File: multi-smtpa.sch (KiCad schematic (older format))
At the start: 72 parts, among them J1 Screw_Terminal_01x02, J10 J SMTPA, J11 Screw_Terminal_01x02, J2 J SMTPA, J3 J SMTPA, J4 J SMTPA, J5 J SMTPA, J6 J SMTPA, J7 J SMTPA, J8 J SMTPA, J9 J SMTPA, U1 LM317L_SO8, U2 LM317L_SO8, U3 LM317L_SO8, U4 LM317L_SO8, U5 LM317L_SO8, U6 LM317L_SO8, U7 LM317L_SO8, U8 LM317L_SO8, U9 LM317L_SO8

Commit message: eval board done
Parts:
- removed F?: Fuse_Small 5A, symbol Device:Fuse_Small
- removed J10, J5, J8, J9: J SMTPA, footprints:SMTPA J30035, symbol Connector_Generic:Conn_01x05
- removed J11, J? (x4): Screw_Terminal_01x02, symbol Connector:Screw_Terminal_01x02
- removed R17, R18: 240R, symbol Device:R
- removed RV8, RV9: R_POT_TRIM, symbol Device:R_POT_TRIM
- removed U5, U9: LM317L_SO8, Package_SO:SOIC-8_3.9x4.9mm_P1.27mm, symbol Regulator_Linear:LM317L_SO8
- added C21, C27, C28, C36, C39, C45, C48, C53, C54: 1n, Capacitor_SMD:C_0603_1608Metric_Pad1.05x0.95mm_HandSolder, symbol Device:C
- added C22: 68p, Capacitor_SMD:C_0603_1608Metric_Pad1.05x0.95mm_HandSolder, symbol Device:C
- added C23, C24, C34, C37, C4, C43, C46, C49, C50, C8: 100n, Capacitor_SMD:C_0603_1608Metric_Pad1.05x0.95mm_HandSolder, symbol Device:C
- added C25, C26, C35, C38, C44, C47, C51, C52: 10n, Capacitor_SMD:C_0603_1608Metric_Pad1.05x0.95mm_HandSolder, symbol Device:C
- added C29, C33, C42: 1u, Capacitor_SMD:C_0805_2012Metric_Pad1.15x1.40mm_HandSolder, symbol Device:C
- added C30, C32, C41: 0.1u, Capacitor_SMD:C_0805_2012Metric_Pad1.15x1.40mm_HandSolder, symbol Device:C
- added C31, C40: 10n, Capacitor_SMD:C_0603_1608Metric_Pad1.05x0.95mm_HandSolder, symbol Device:C_Small
- added C55, C57: 100p, Capacitor_SMD:C_0402_1005Metric, symbol Device:C
- added C56, C58: 10p, Capacitor_SMD:C_0402_1005Metric, symbol Device:C
- added D2, D3, D4, D5, D6, D7: D_Schottky_x2_Serial_AKC, Package_TO_SOT_SMD:SOT-23, symbol Device:D_Schottky_x2_Serial_AKC
- added H1, H2, H3, H4: MountingHole, MountingHole:MountingHole_4.3mm_M4_DIN965_Pad, symbol Mechanical:MountingHole
- added J10, J13, J15, J18, J19, J21, J5, J8, J9: Conn_Coaxial, Connector_Coaxial:SMA_Amphenol_132289_EdgeMount, symbol Connector:Conn_Coaxial
- added J11, J12, J14, J16, J17, J20: J SMTPA, footprints:SMTPA J30035, symbol Connector_Generic:Conn_01x05
- added L1: 43n, Inductor_SMD:L_0402_1005Metric, symbol Device:L
- added U5: ADL5610, Package_TO_SOT_SMD:SOT-89-3, symbol RF_Amplifier:ADL5610
- C1, C12, C2, C3, C5, C6, C7, C9: footprint (none) -> Capacitor_SMD:C_0805_2012Metric_Pad1.15x1.40mm_HandSolder
- C10: value 0.1u -> 100n; footprint (none) -> Capacitor_SMD:C_0603_1608Metric_Pad1.05x0.95mm_HandSolder
- C11: value 0.1u -> 2u2T; footprint (none) -> Capacitor_SMD:C_0805_2012Metric_Pad1.15x1.40mm_HandSolder
- C13, C14: value 1u -> 10n; footprint (none) -> Capacitor_SMD:C_0603_1608Metric_Pad1.05x0.95mm_HandSolder
- C15: value 0.1u -> 10n; footprint (none) -> Capacitor_SMD:C_0603_1608Metric_Pad1.05x0.95mm_HandSolder
- C16: value 0.1u -> 1.2n; footprint (none) -> Capacitor_SMD:C_0603_1608Metric_Pad1.05x0.95mm_HandSolder
- C17: value 0.1u -> 100p; footprint (none) -> Capacitor_SMD:C_0603_1608Metric_Pad1.05x0.95mm_HandSolder
- C18: value 1u -> 100p; footprint (none) -> Capacitor_SMD:C_0603_1608Metric_Pad1.05x0.95mm_HandSolder
- C19, C20: value 1u -> 1n; footprint (none) -> Capacitor_SMD:C_0603_1608Metric_Pad1.05x0.95mm_HandSolder
- D1: footprint (none) -> Diode_THT:D_A-405_P10.16mm_Horizontal
- F1: renamed from F?; value Fuse_Small -> Fuse 1A fast; footprint (none) -> Resistor_THT:R_Axial_DIN0207_L6.3mm_D2.5mm_P10.16mm_Horizontal
- J1: footprint (none) -> TerminalBlock_TE-Connectivity:TerminalBlock_TE_282834-2_1x02_P2.54mm_Horizontal
- R1, R10, R15, R16, R2, R3, R4, R5, R6, R7: footprint (none) -> Resistor_SMD:R_0805_2012Metric_Pad1.15x1.40mm_HandSolder
- R11: value 240R -> 1K0; footprint (none) -> Resistor_SMD:R_0603_1608Metric_Pad1.05x0.95mm_HandSolder
- R12: value 240R -> 1K0; footprint (none) -> Resistor_SMD:R_0805_2012Metric_Pad1.15x1.40mm_HandSolder
- R13, R9: value 1K0 -> 240R; footprint (none) -> Resistor_SMD:R_0805_2012Metric_Pad1.15x1.40mm_HandSolder
- R14: footprint (none) -> Resistor_SMD:R_0603_1608Metric_Pad1.05x0.95mm_HandSolder
- R8: value 1K0 -> 22R; footprint (none) -> Resistor_SMD:R_0603_1608Metric_Pad1.05x0.95mm_HandSolder
- RV1, RV2, RV3, RV4, RV5, RV6, RV7: footprint (none) -> Potentiometer_THT:Potentiometer_Bourns_3006Y_Horizontal
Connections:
- net VDC_22 is gone; now on net VDC_10: C20.1
- net +48V: now also D1.2 (A), C30.1, C32.1, C41.1; no longer C10.1, C11.1, C15.1, C16.1, C17.1, D1.1 (K)
- net Fast_00: now also J5.1 (In)
- net Fast_01: now also J10.1 (In)
- net Fast_10: now also D3.3 (common)
- net Fast_11: now also D2.3 (common)
- net Fast_20: now also C17.2
- net Fast_21: now also J17.2 (Pin_2), J18.1 (In)
- net Fast_22: now also J19.1 (In), J20.2 (Pin_2)
- net GND: now also C11.1, C14.2, C15.2, C16.1, C19.2, C20.2, C3.2, C7.2, R12.2, R15.2, R3.2, RV5.3, C21.2, C22.1, C23.2, C24.2, C25.2, C26.2, C27.2, C28.2, C29.2, C30.2, C32.2, C33.2, C34.2, C35.2, C36.2, C37.2, C38.2, C39.2, C4.2, C41.2, C42.2, C43.2, C44.2, C45.2, C46.2, C47.2, C48.2, C49.2, C50.2, C51.2, C52.2, C53.2, C54.2, C55.2, C56.2, C57.2, C58.2, C8.2, D2.1 (A), D3.1 (A), D4.1 (A), D5.1 (A), D6.1 (A), D7.1 (A), J10.2 (Ext), J11.1 (Pin_1), J11.4 (Pin_4), J11.5 (Pin_5), J12.1 (Pin_1), J12.4 (Pin_4), J12.5 (Pin_5), J13.2 (Ext), J14.1 (Pin_1), J14.4 (Pin_4), J14.5 (Pin_5), J15.2 (Ext), J16.1 (Pin_1), J16.4 (Pin_4), J16.5 (Pin_5), J17.1 (Pin_1), J17.4 (Pin_4), J17.5 (Pin_5), J18.2 (Ext), J19.2 (Ext), J20.1 (Pin_1), J20.4 (Pin_4), J20.5 (Pin_5), J21.2 (Ext), J5.2 (Ext), J8.2 (Ext), J9.2 (Ext), U5.2 (GND); no longer R8.2
- net VDC_00: now also C13.1, C19.1, C4.1, C55.1, C56.1
- net VDC_01: now also C23.1, C25.1, C27.1
- net VDC_10: now also C14.1, J7.3 (Pin_3), C24.1, C26.1, C28.1, C8.1
- net VDC_20: now also C10.1, C15.1, C21.1
- net VDC_21: now also R13.2, U7.2 (VO), U7.3 (VO), U7.6 (VO), U7.7 (VO), C33.1, C34.1, C35.1, C36.1, C37.1, C38.1, C39.1, C57.1, C58.1, J17.3 (Pin_3), J20.3 (Pin_3); no longer C14.1, R12.2, U6.2 (VO), U6.3 (VO), U6.6 (VO), U6.7 (VO)
- net at RV5.2: now also R9.1, U6.4 (ADJ); no longer R11.1
- net TEEBFast_20: now reaches R8.1
- net TEEBFast_20: now also R9.2, U6.2 (VO), U6.3 (VO), U6.6 (VO), U6.7 (VO), C29.1; no longer RV5.3
- net at RV6.3: now also R12.1; no longer R9.1
- net at R16.1, RV7.2: now also U8.4 (ADJ); no longer U7.4 (ADJ)
- net at R13.1: now also RV6.2, U7.4 (ADJ); no longer RV7.3
- net VssFast_lin: now reaches R14.1
- net VssFast_lin: now also J21.1 (In)
- net at R15.1: now also RV7.3
- net at F1.1: now also D1.1 (K); no longer D1.2 (A)
- removed net VDC_02: C18.1, R16.2, U7.2 (VO), U7.3 (VO), U7.6 (VO), U7.7 (VO)
- removed net VDC_11: C13.1, J7.3 (Pin_3), R11.2
- net VDC_12 renamed VDC_lin
- net VDC_lin: now also R16.2, C42.1, C43.1, C44.1, C45.1, C46.1, C47.1, C48.1, C49.1, C50.1, C51.1, C52.1, C53.1, C54.1, J11.3 (Pin_3), J12.3 (Pin_3), J14.3 (Pin_3), J16.3 (Pin_3); no longer C19.1
- new net AFast_20: C18.2, J8.1 (In)
- new net ATEEFast_20: C18.1, L1.2, U5.3
- new net CFast_1X: C31.1, J9.1 (In)
- new net CFast_lin: C40.1, J13.1 (In)
- new net Fast_1X: C31.2, D2.2 (K), D3.2 (K), R11.2
- new net Fast_lin: C40.2, D4.2 (K), D5.2 (K), D6.2 (K), D7.2 (K), R14.2
- new net Fast_lin0: D4.3 (common), J11.2 (Pin_2)
- new net Fast_lin1: D5.3 (common), J14.2 (Pin_2)
- new net Fast_lin2: D6.3 (common), J12.2 (Pin_2)
- new net Fast_lin3: D7.3 (common), J16.2 (Pin_2)
- new net PAFast_20: C17.1, U5.1
- new net TEEAFast_20: C11.2, C16.2, C22.2, L1.1, R8.2
- new net VssFast_1X: J15.1 (In), R11.1
- no-connect marks 9 -> 7
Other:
- note added: "Amplified Output"
- note added: "Linear Array of Four SiPMs, Signal Mux'd with Diodes, Tight Pack"
- note added: "Power"
- note added: "Sbias voltage and this applies a forward bias across the Schottky diodes.\n A 1kOhm resistor, Rs, is placed in series with Sbias at the Common Readout node.\nThe bias voltage is adjusted such that an optimal standing current of <1mA per Shottky diode is set up."
- note added: "Single SiPM, Amplified Output Experiment"
- note added: "Two SiPMs Mux'd with Diodes Experiment, Diode Under SiPM"
- note added: "Two SiPMs, One Power Source Experiment"
- note added: "Two SiPMs, individual Power Source, Differing Caps & Layout Experiment"
- note added: "approx 50 mA max @ 28V PER SiPM\napprox 14 Watts @ 0.5A total"
- note removed: "apply variable voltage 5-12.6V \nfan 603-1025-ND\n500mA"
- note removed: "approx 50 mA max @ 28V\napprox 14 Watts @ 0.5A total"
- moved on the sheet: C1, C12, C2, C3, C5, C6, C7, C9, D1, F1, J1, J2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

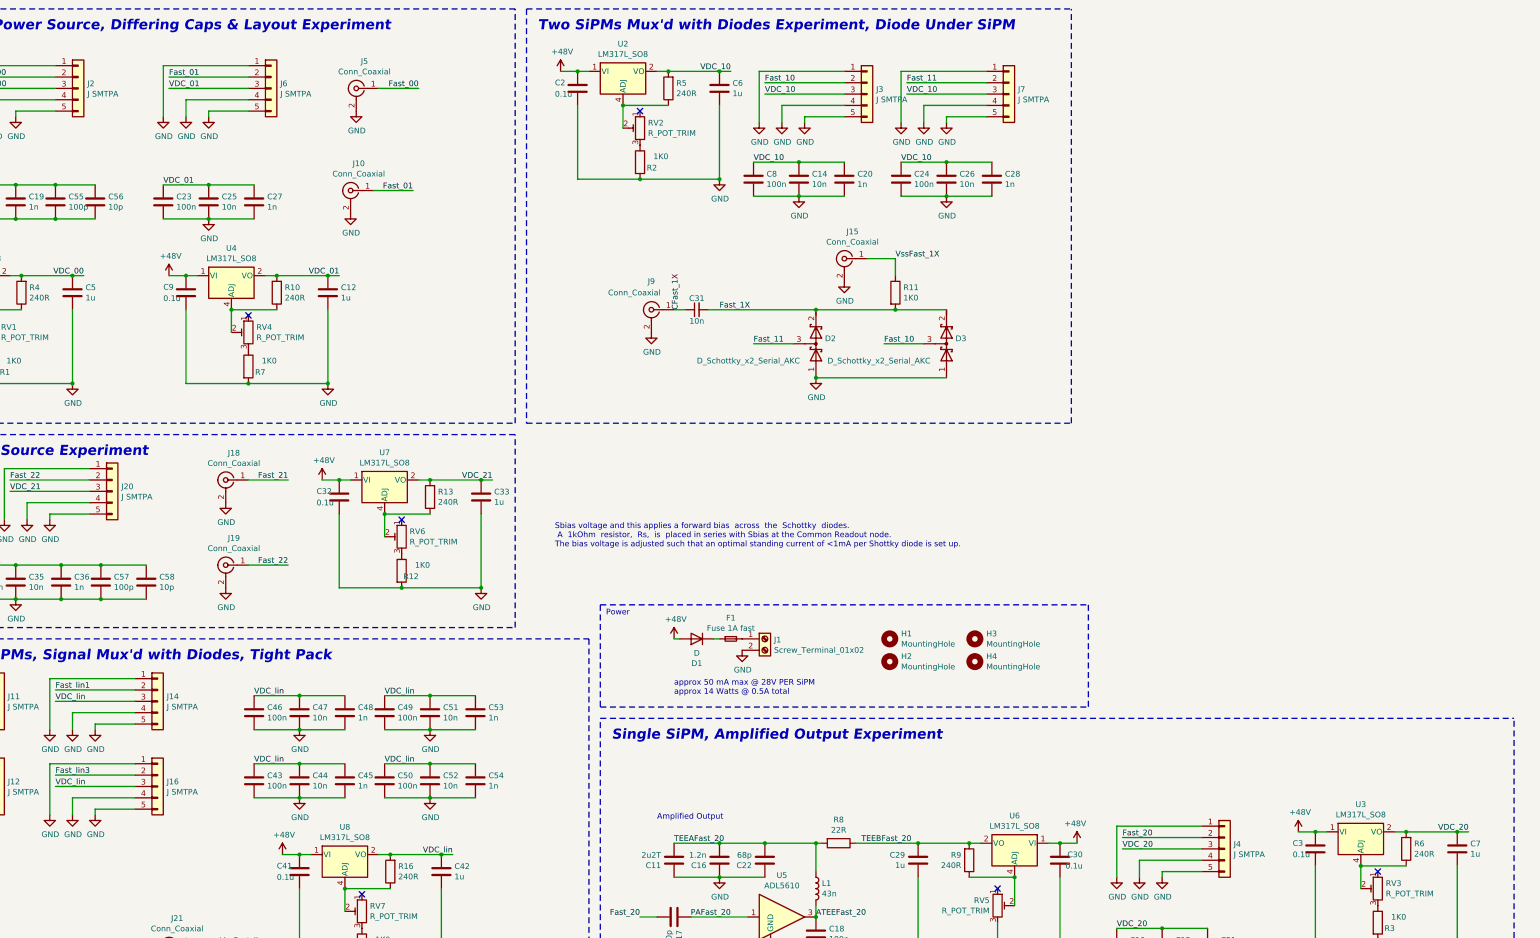
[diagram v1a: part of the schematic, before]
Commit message: added another experiment, testpoints, fiducials
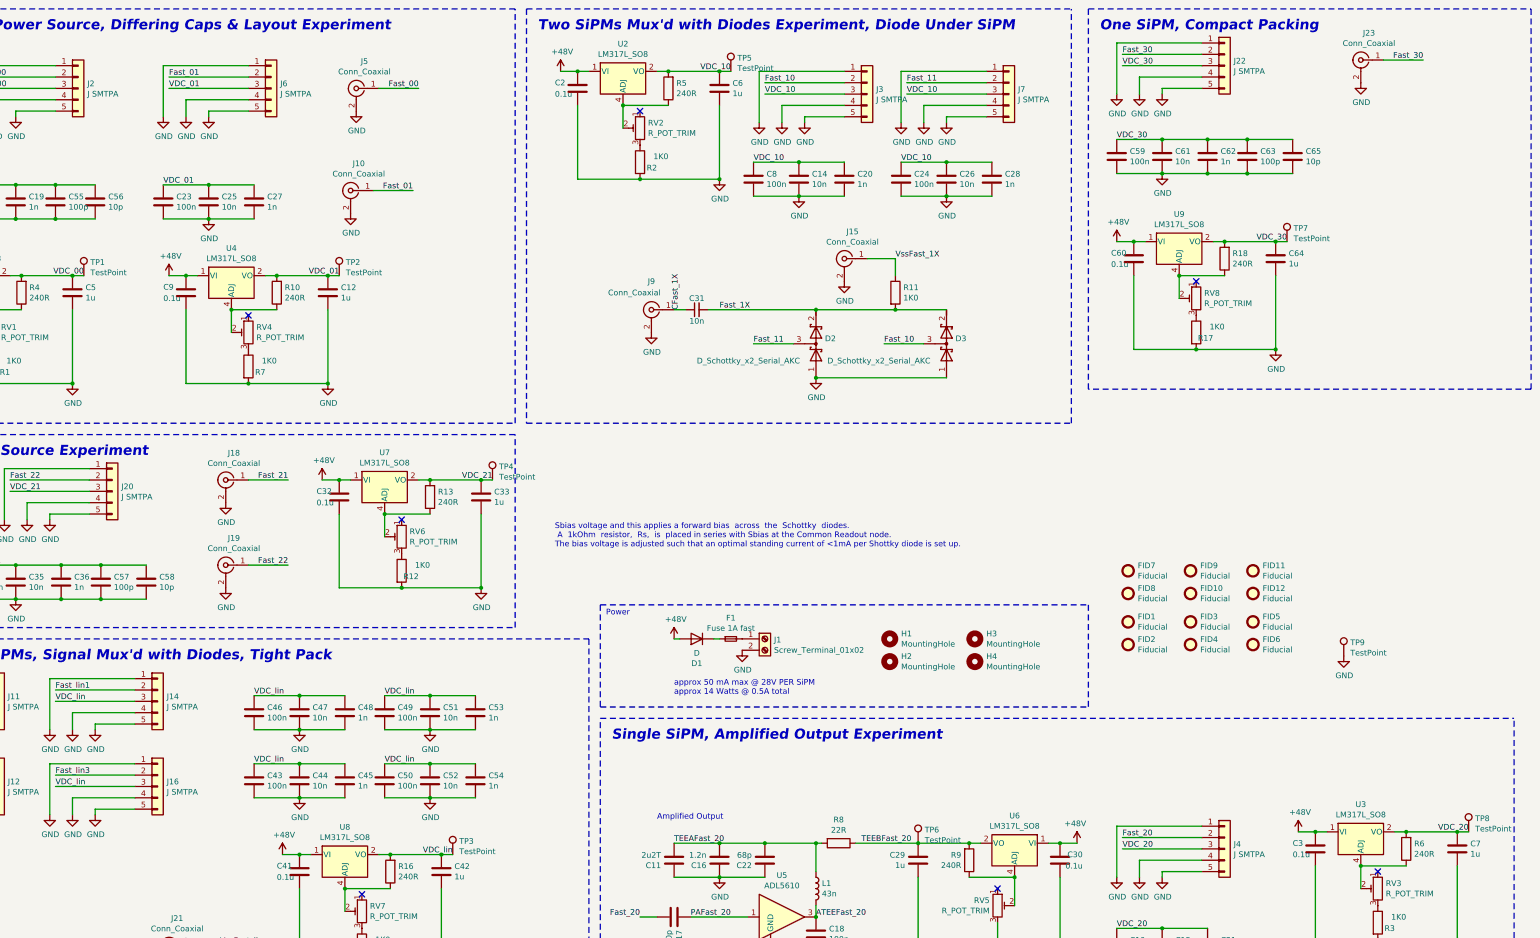
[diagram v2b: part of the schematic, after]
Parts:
- added C59: 100n, Capacitor_SMD:C_0603_1608Metric_Pad1.05x0.95mm_HandSolder, symbol Device:C
- added C60: 0.1u, Capacitor_SMD:C_0805_2012Metric_Pad1.15x1.40mm_HandSolder, symbol Device:C
- added C61: 10n, Capacitor_SMD:C_0603_1608Metric_Pad1.05x0.95mm_HandSolder, symbol Device:C
- added C62: 1n, Capacitor_SMD:C_0603_1608Metric_Pad1.05x0.95mm_HandSolder, symbol Device:C
- added C63: 100p, Capacitor_SMD:C_0402_1005Metric, symbol Device:C
- added C64: 1u, Capacitor_SMD:C_0805_2012Metric_Pad1.15x1.40mm_HandSolder, symbol Device:C
- added C65: 10p, Capacitor_SMD:C_0402_1005Metric, symbol Device:C
- added FID1, FID10, FID11, FID12, FID2, FID3, FID4, FID5, FID6, FID7, FID8, FID9: Fiducial, Fiducial:Fiducial_1mm_Mask3mm, symbol Mechanical:Fiducial
- added J22: J SMTPA, footprints:SMTPA J30035, symbol Connector_Generic:Conn_01x05
- added J23: Conn_Coaxial, Connector_Coaxial:SMA_Amphenol_132289_EdgeMount, symbol Connector:Conn_Coaxial
- added R17: 1K0, Resistor_SMD:R_0805_2012Metric_Pad1.15x1.40mm_HandSolder, symbol Device:R
- added R18: 240R, Resistor_SMD:R_0805_2012Metric_Pad1.15x1.40mm_HandSolder, symbol Device:R
- added RV8: R_POT_TRIM, Potentiometer_SMD:Potentiometer_Bourns_3314G_Vertical, symbol Device:R_POT_TRIM
- added TP1, TP2, TP3, TP4, TP5, TP6, TP7, TP8: TestPoint, TestPoint:TestPoint_Pad_D2.0mm, symbol Connector:TestPoint
- added TP9: TestPoint, TestPoint:TestPoint_Pad_4.0x4.0mm, symbol Connector:TestPoint
- added U9: LM317L_SO8, Package_SO:SOIC-8_3.9x4.9mm_P1.27mm, symbol Regulator_Linear:LM317L_SO8
- H1, H2, H3, H4: footprint MountingHole:MountingHole_4.3mm_M4_DIN965_Pad -> MountingHole:MountingHole_4.3mm_M4_Pad_Via
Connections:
- net +48V: now also C60.1, U9.1 (VI)
- net GND: now also C59.2, C60.2, C61.2, C62.2, C63.2, C64.2, C65.2, J22.1 (Pin_1), J22.4 (Pin_4), J22.5 (Pin_5), J23.2 (Ext), R17.2, TP9.1
- net TEEBFast_20: now also TP6.1
- net VDC_00: now also TP1.1
- net VDC_01: now also TP2.1
- net VDC_10: now also TP5.1
- net VDC_20: now also TP8.1
- net VDC_21: now also TP4.1
- net VDC_lin: now also TP3.1
- new net: R18.1, RV8.2, U9.4 (ADJ)
- new net: R17.1, RV8.3
- new net Fast_30: J22.2 (Pin_2), J23.1 (In)
- new net VDC_30: C59.1, C61.1, C62.1, C63.1, C64.1, C65.1, J22.3 (Pin_3), R18.2, TP7.1, U9.2 (VO), U9.3 (VO), U9.6 (VO), U9.7 (VO)
- no-connect marks 7 -> 8
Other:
- note added: "One SiPM, Compact Packing"
